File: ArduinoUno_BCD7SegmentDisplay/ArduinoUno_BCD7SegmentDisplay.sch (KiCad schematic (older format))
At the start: 18 parts, among them P1 Power, P2 Analog, P3 Digital, P4 Digital, P5 CONN_01X01, P6 CONN_01X01, P7 CONN_01X01, P8 CONN_01X01, SW1 SW_Push, U1 74LS47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

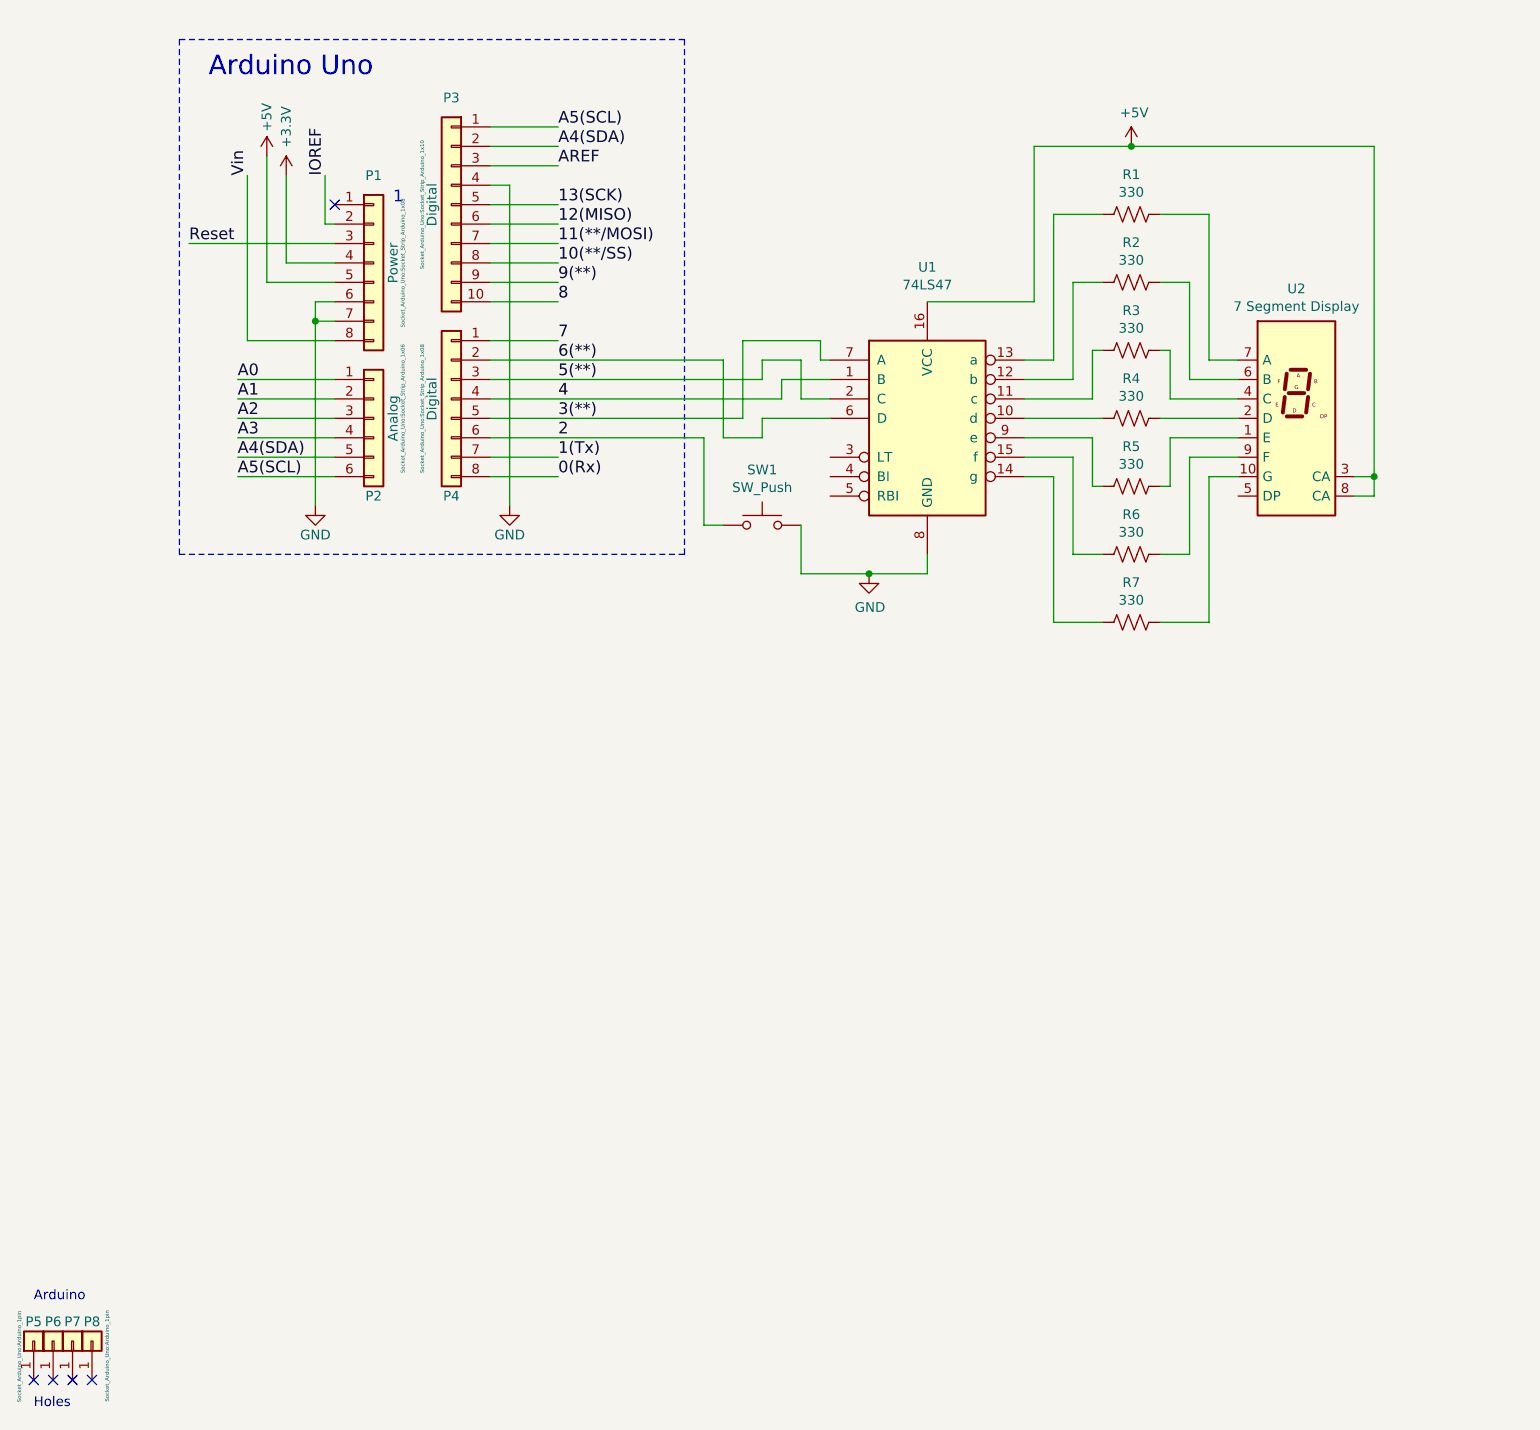
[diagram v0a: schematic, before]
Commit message: Added bypass capacitor to schematic and removed ISR from program.
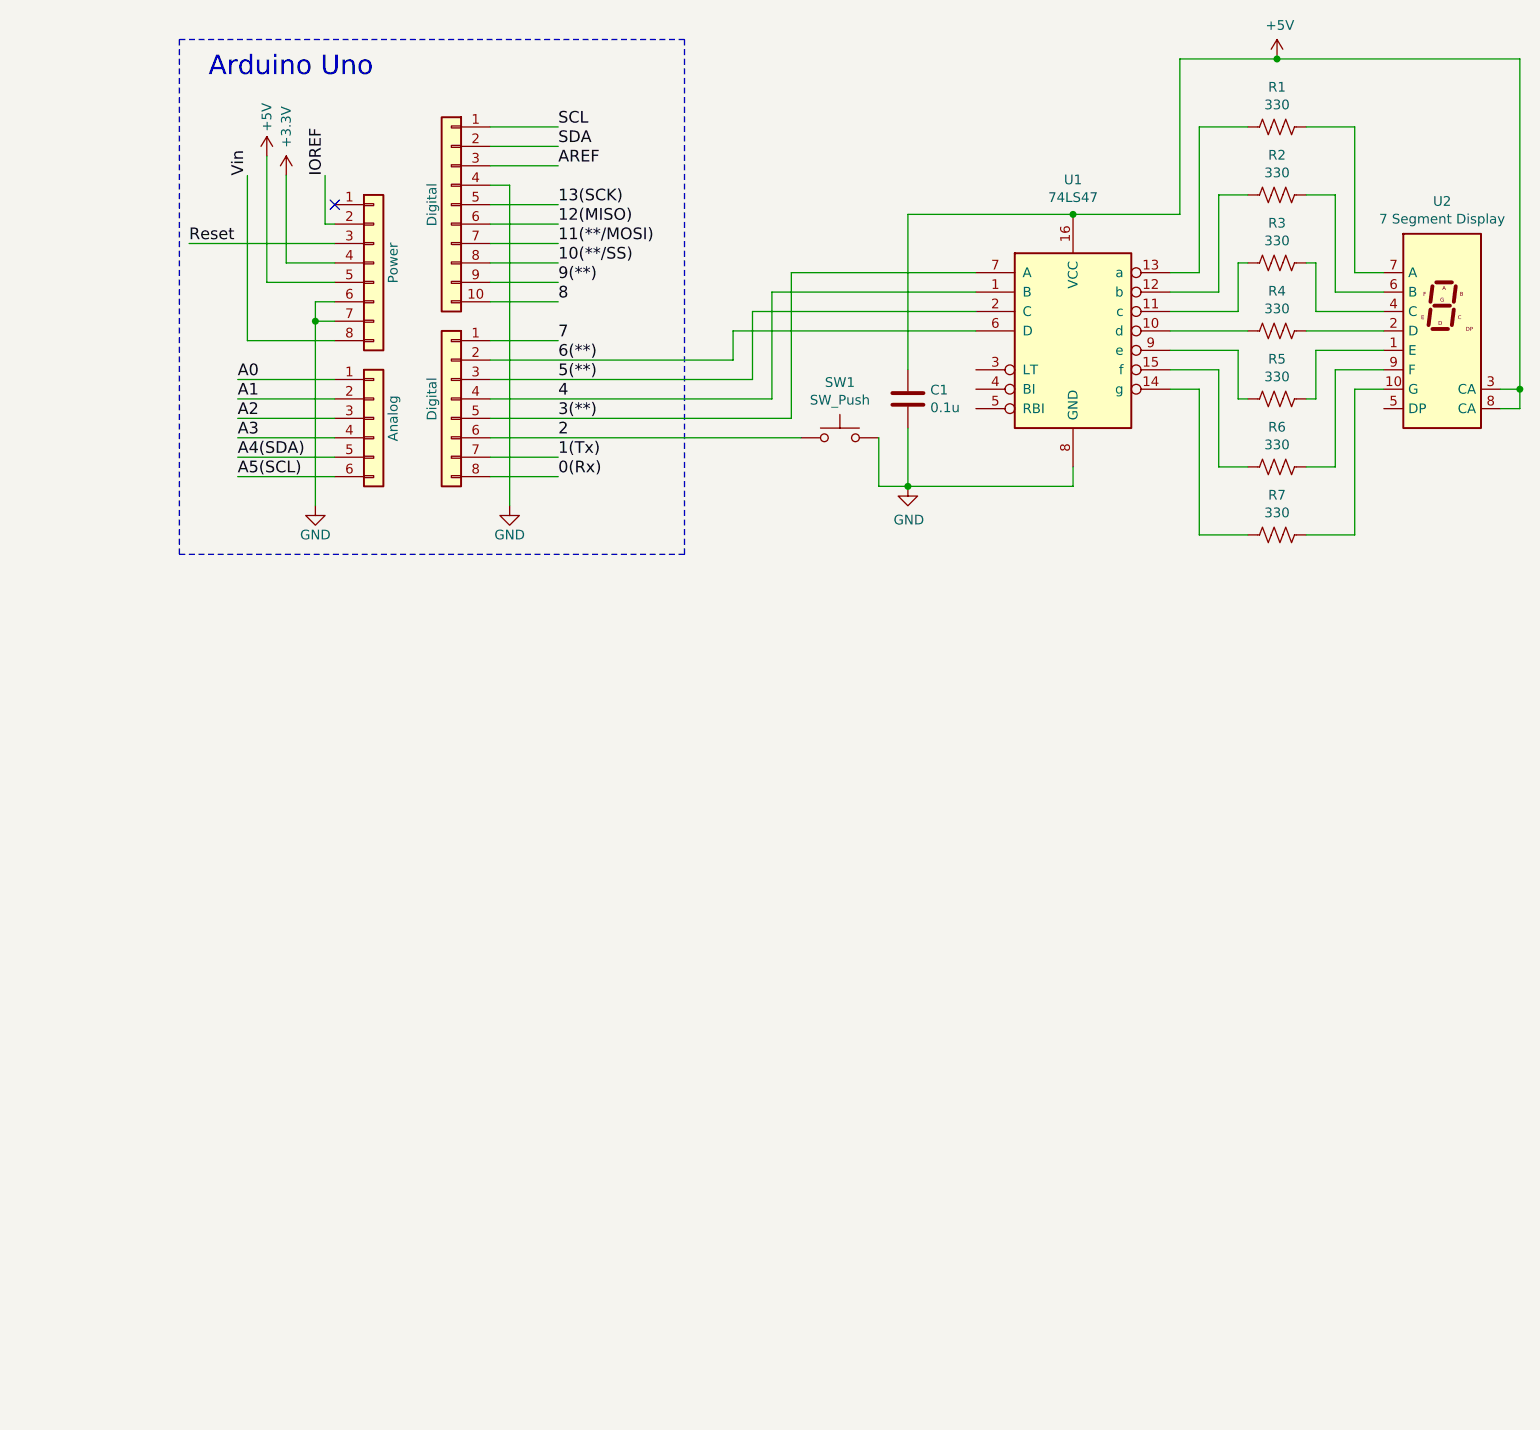
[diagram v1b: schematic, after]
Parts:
- removed P5, P6, P7, P8: CONN_01X01, Socket_Arduino_Uno:Arduino_1pin, symbol Connector_Generic:Conn_01x01
- added C1: 0.1u, symbol Device:C
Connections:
- net +5V: now also C1.1
- net A4(SDA): no longer P3.2 (Pin_2)
- net A5(SCL): no longer P3.1 (Pin_1)
- net GND: now also C1.2
- new net SCL: P3.1 (Pin_1)
- new net SDA: P3.2 (Pin_2)
- no-connect marks 5 -> 1
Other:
- note removed: "1"
- note removed: "Arduino"
- note removed: "Holes"
- moved on the sheet: R1, R2, R3, R4, R5, R6, R7, SW1, U1, U2
